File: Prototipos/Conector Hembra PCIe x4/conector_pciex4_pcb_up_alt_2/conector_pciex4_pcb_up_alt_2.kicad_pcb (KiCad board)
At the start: 2 copper layers, 50 x 18 mm, 33 parts, among them J1 10018783-10211TLF

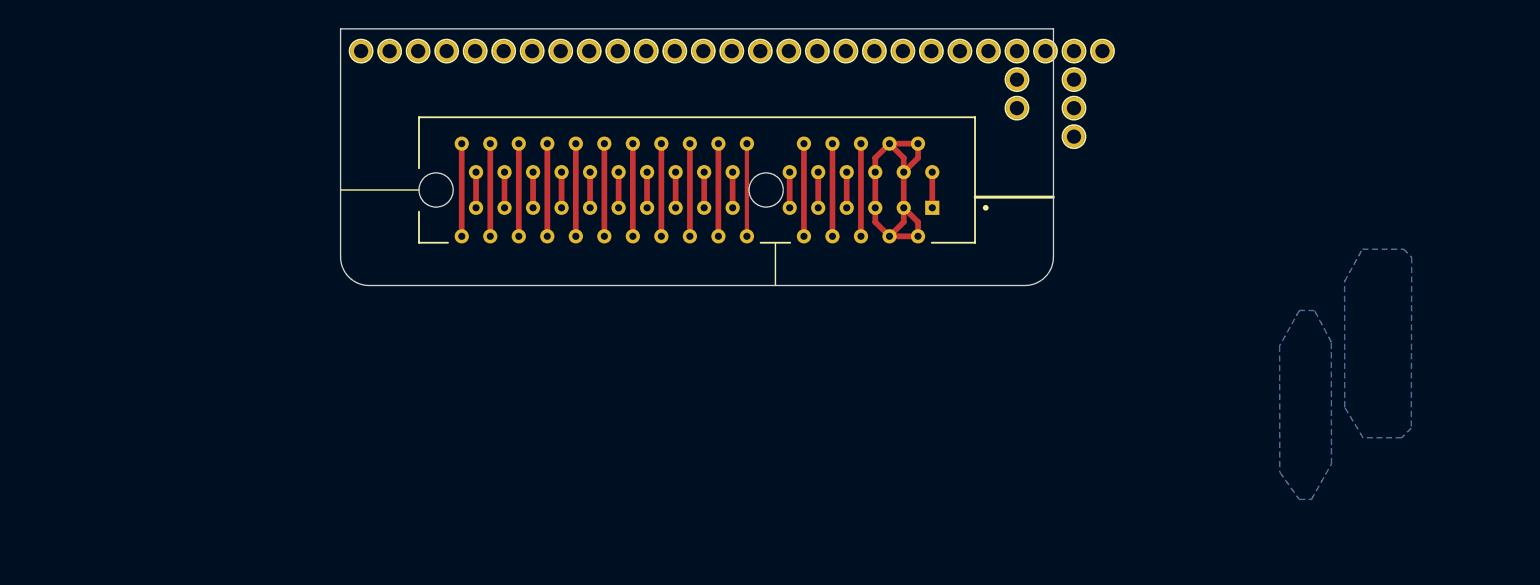
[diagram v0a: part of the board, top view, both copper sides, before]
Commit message: Agregar nuevas versiones trazas 0.4mm y 0.3mm
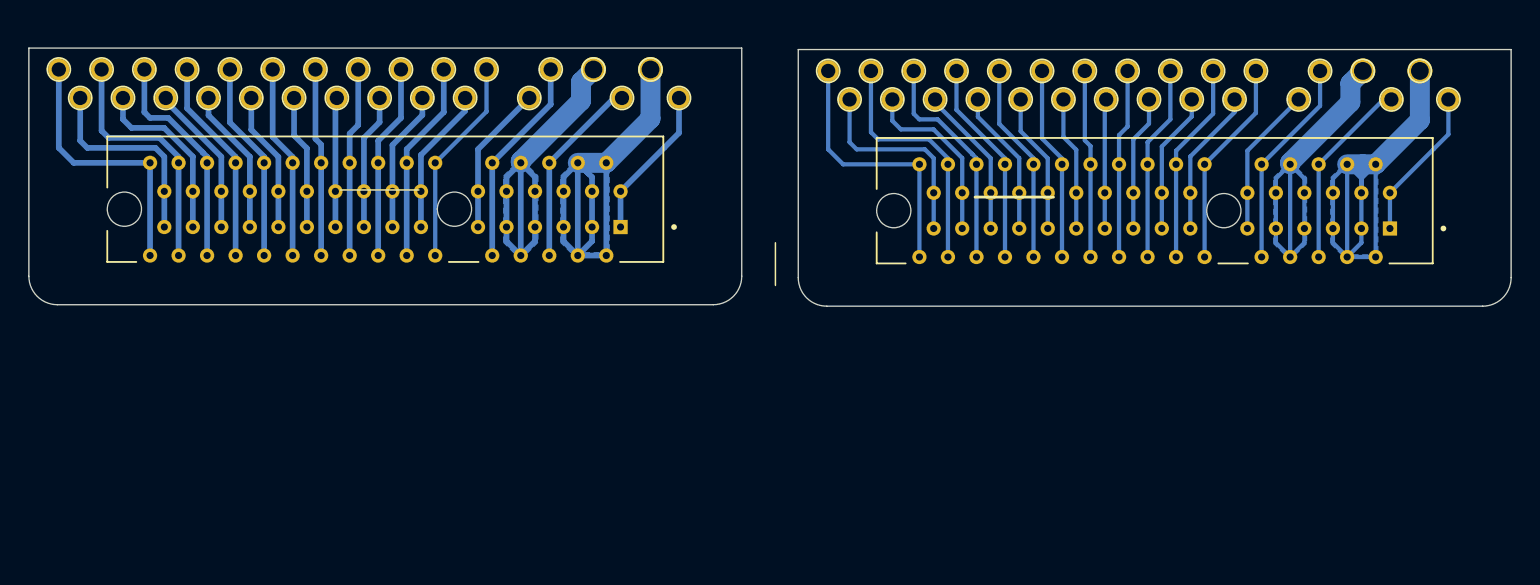
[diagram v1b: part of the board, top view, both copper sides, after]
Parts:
- removed TP3, TP4, TP5: PGND, pin_hole_pcie:TestPoint_THTPad_D1.5mm_Drill0.7mm
- removed TP8, TP9: 12Vdc, pin_hole_pcie:TestPoint_THTPad_D1.5mm_Drill0.7mm
- added J1: 10018783-10211TLF, KiCad-Libraries:AMPHENOL_PCIe-x4_10018783-10211TLF, F.Cu at (179.8, 92.8)
- added TP1: HP_Power, pin_hole_pcie:TestPoint_THTPad_D1.5mm_Drill0.7mm, F.Cu at (195.6, 85.0)
- added TP10: 48Vac_L, pin_hole_pcie:TestPoint_THTPad_D1.5mm_Drill0.7mm, F.Cu at (186.6, 83.0)
- added TP11: 48Vac_N, pin_hole_pcie:TestPoint_THTPad_D1.5mm_Drill0.7mm, F.Cu at (185.1, 85.0)
- added TP12: AGND, pin_hole_pcie:TestPoint_THTPad_D1.5mm_Drill0.7mm, F.Cu at (182.1, 83.0)
- added TP13: 3,3Vdc_Signal, pin_hole_pcie:TestPoint_THTPad_D1.5mm_Drill0.7mm, F.Cu at (180.6, 85.0)
- added TP14: S1, pin_hole_pcie:TestPoint_THTPad_D1.5mm_Drill0.7mm, F.Cu at (179.1, 83.0)
- added TP15: S2, pin_hole_pcie:TestPoint_THTPad_D1.5mm_Drill0.7mm, F.Cu at (177.6, 85.0)
- added TP16: S3, pin_hole_pcie:TestPoint_THTPad_D1.5mm_Drill0.7mm, F.Cu at (176.1, 83.0)
- added TP17: S4, pin_hole_pcie:TestPoint_THTPad_D1.5mm_Drill0.7mm, F.Cu at (174.6, 85.0)
- added TP18: S5, pin_hole_pcie:TestPoint_THTPad_D1.5mm_Drill0.7mm, F.Cu at (173.1, 83.0)
- added TP19: S6, pin_hole_pcie:TestPoint_THTPad_D1.5mm_Drill0.7mm, F.Cu at (171.6, 85.0)
- added TP2: PGND, pin_hole_pcie:TestPoint_THTPad_D1.5mm_Drill0.7mm, F.Cu at (193.6, 83.0)
- added TP20: S7, pin_hole_pcie:TestPoint_THTPad_D1.5mm_Drill0.7mm, F.Cu at (170.1, 83.0)
- added TP21: S8, pin_hole_pcie:TestPoint_THTPad_D1.5mm_Drill0.7mm, F.Cu at (168.6, 85.0)
- added TP22: S9, pin_hole_pcie:TestPoint_THTPad_D1.5mm_Drill0.7mm, F.Cu at (167.1, 83.0)
- added TP23: S10, pin_hole_pcie:TestPoint_THTPad_D1.5mm_Drill0.7mm, F.Cu at (165.6, 85.0)
- added TP24: S11, pin_hole_pcie:TestPoint_THTPad_D1.5mm_Drill0.7mm, F.Cu at (164.1, 83.0)
- added TP25: S12, pin_hole_pcie:TestPoint_THTPad_D1.5mm_Drill0.7mm, F.Cu at (162.6, 85.0)
- added TP26: S13, pin_hole_pcie:TestPoint_THTPad_D1.5mm_Drill0.7mm, F.Cu at (161.1, 83.0)
- added TP27: S14, pin_hole_pcie:TestPoint_THTPad_D1.5mm_Drill0.7mm, F.Cu at (159.6, 85.0)
- added TP28: S15, pin_hole_pcie:TestPoint_THTPad_D1.5mm_Drill0.7mm, F.Cu at (158.1, 83.0)
- added TP29: S16, pin_hole_pcie:TestPoint_THTPad_D1.5mm_Drill0.7mm, F.Cu at (156.6, 85.0)
- added TP30: MODULE_IDENT, pin_hole_pcie:TestPoint_THTPad_D1.5mm_Drill0.7mm, F.Cu at (155.1, 83.0)
- added TP31: AGND, pin_hole_pcie:TestPoint_THTPad_D1.5mm_Drill0.7mm, F.Cu at (153.6, 85.0)
- added TP32: HP_Signal, pin_hole_pcie:TestPoint_THTPad_D1.5mm_Drill0.7mm, F.Cu at (152.1, 83.0)
- added TP6: 5Vdc, pin_hole_pcie:TestPoint_THTPad_D1.5mm_Drill0.7mm, F.Cu at (191.6, 85.0)
- added TP7: 12Vdc, pin_hole_pcie:TestPoint_THTPad_D1.5mm_Drill0.7mm, F.Cu at (189.6, 83.0)
- moved TP12 31.2 mm to (128.1, 82.8)
- moved TP13 30.9 mm to (126.6, 84.8)
- moved TP10 30.7 mm to (132.6, 82.8)
- moved TP11 30.4 mm to (131.1, 84.8)
- moved TP14 30.2 mm to (125.1, 82.8)
- moved TP15 29.9 mm to (123.6, 84.8)
- moved TP1 29.9 mm to (141.6, 84.8)
- moved TP6 29.9 mm to (137.6, 84.8)
- moved TP2 29.8 mm to (139.6, 82.8)
- moved TP7 29.8 mm to (135.6, 82.8)
- moved TP16 29.2 mm to (122.1, 82.8)
- moved TP17 28.9 mm to (120.6, 84.8)
- moved TP18 28.2 mm to (119.1, 82.8)
- moved TP19 27.9 mm to (117.6, 84.8)
- moved TP20 27.2 mm to (116.1, 82.8)
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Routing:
- net Net-(J1-PadA2): track 23.5 -> 83.0 mm
- net Net-(J1-PadA7): track 11.5 -> 59.6 mm
- net Net-(J1-PadA32): track 6.50 -> 36.7 mm
- net Net-(J1-PadA30): track 6.50 -> 34.8 mm
- net Net-(J1-PadA31): track 2.50 -> 28.6 mm
- net Net-(J1-PadA28): track 6.50 -> 31.2 mm
- net Net-(J1-PadA10): track 6.50 -> 29.5 mm
- net Net-(J1-PadA12): track 6.50 -> 29.1 mm
- net Net-(J1-PadA26): track 6.50 -> 28.9 mm
- net Net-(J1-PadA29): track 2.50 -> 24.8 mm
- net Net-(J1-PadA14): track 6.50 -> 28.3 mm
- net Net-(J1-PadA24): track 6.50 -> 28.1 mm
- net Net-(J1-PadA16): track 6.50 -> 27.4 mm
- net Net-(J1-PadA22): track 6.50 -> 27.3 mm
- net Net-(J1-PadA6): track 6.50 -> 27.0 mm
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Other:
- board size 50 x 18 mm -> 104 x 18.1 mm
